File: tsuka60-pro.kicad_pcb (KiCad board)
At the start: 2 copper layers, 285 x 94.6 mm, 171 parts, among them J1 USB_C_Receptacle_USB2.0, J2 Conn_01x04_MountingPin, SW1 SW_Reset, U1 ATmega32U4-M, U2 SRV05-4, Y1 16MHz

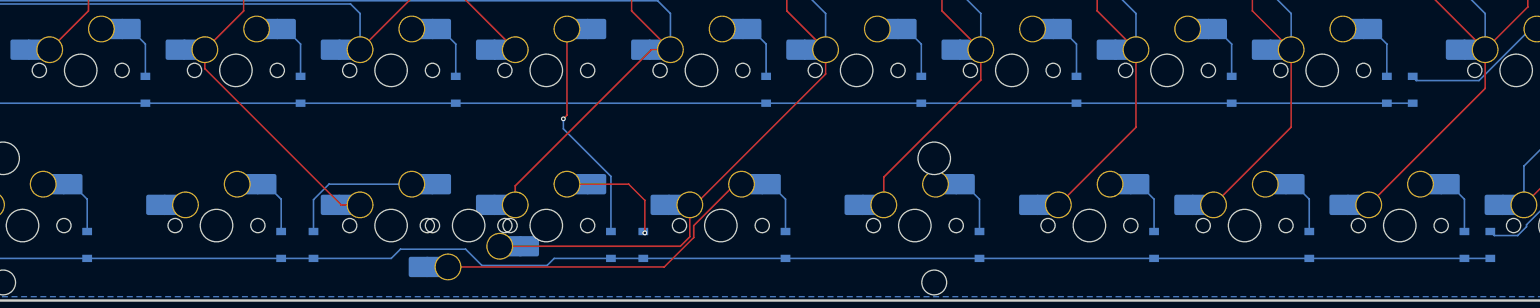
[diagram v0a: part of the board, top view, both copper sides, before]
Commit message: Add missing trace
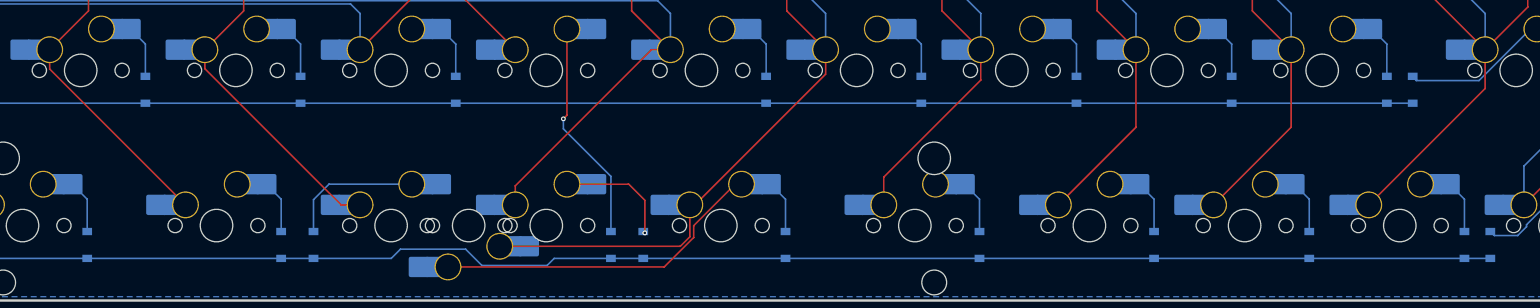
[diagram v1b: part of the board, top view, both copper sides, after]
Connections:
- MX66 pad 1: unconnected-(MX66-Pad1) -> COL5
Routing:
- net COL5: track 132.1 -> 158.1 mm

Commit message: Repair BOM, update USB-C component, footprint and placement
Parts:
- J1: footprint marbastlib-various:USB_C_Receptacle_HRO_TYPE-C-31-M-14 -> Connector_USB:USB_C_Receptacle_HRO_TYPE-C-31-M-12
- R3, R4: value 5k -> 5.1k
- moved J1 3.86 mm to (82.1, 82.2)
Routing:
- net GND: track 105.8 -> 95.2 mm, vias 2 -> 0
- net Net-(J1-PadA5): track 8.67 -> 12.4 mm
- net VCC: track 22.4 -> 24.0 mm
- net D+: track 36.5 -> 37.8 mm
- net Net-(J1-PadB5): track 8.40 -> 7.70 mm, vias 2 -> 0
- net D-: track 37.6 -> 38.1 mm
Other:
- outline, holes or cut-outs redrawn

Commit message: Update some traces
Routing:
- net Net-(D69-Pad2): track 14.6 -> 11.8 mm
- net COL9: track 294.7 -> 296.4 mm
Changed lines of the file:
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@@
   (segment (start 187.325 161.922183) (end 187.325 165.83125) (width 0.2) (layer "B.Cu") (net 65))
   (segment (start 199.39 160.02) (end 189.227183 160.02) (width 0.2) (layer "B.Cu") (net 65))
-  (segment (start 218.44 151.56) (end 218 152) (width 0.2) (layer "F.Cu") (net 66))
-  (segment (start 218.44 140.97) (end 218.44 151.56) (width 0.2) (layer "F.Cu") (net 66))
-  (via (at 218 152) (size 0.6) (drill 0.3) (layers "F.Cu" "B.Cu") (net 66))
-  (segment (start 223.8375 165.83125) (end 223.8375 159.064683) (width 0.2) (layer "B.Cu") (net 66))
-  (segment (start 223.8375 159.064683) (end 218 153.227183) (width 0.2) (layer "B.Cu") (net 66))
-  (segment (start 218 153.227183) (end 218 152) (width 0.2) (layer "B.Cu") (net 66))
-  (segment (start 228 162) (end 226.02 160.02) (width 0.2) (layer "F.Cu") (net 67))
-  (segment (start 228 166) (end 228 162) (width 0.2) (layer "F.Cu") (net 67))
-  (segment (start 226.02 160.02) (end 218.44 160.02) (width 0.2) (layer "F.Cu") (net 67))
-  (via (at 228 166) (size 0.6) (drill 0.3) (layers "F.Cu" "B.Cu") (net 67))
-  (segment (start 227.83125 165.83125) (end 228 166) (width 0.2) (layer "B.Cu") (net 67))
-  (segment (start 227.80625 165.83125) (end 227.83125 165.83125) (width 0.2) (layer "B.Cu") (net 67))
+  (segment (start 218.44 140.97) (end 218.44 151.46) (width 0.2) (layer "F.Cu") (net 66))
+  (segment (start 218.44 151.46) (end 218.44 151.94) (width 0.2) (layer "F.Cu") (net 66))
+  (via (at 218.44 151.94) (size 0.6) (drill 0.3) (layers "F.Cu" "B.Cu") (net 66))
+  (segment (start 223.8375 165.83125) (end 223.8375 159.6625) (width 0.2) (layer "B.Cu") (net 66))
+  (segment (start 223.8375 157.3375) (end 218.44 151.94) (width 0.2) (layer "B.Cu") (net 66))
+  (segment (start 223.8375 159.6625) (end 223.8375 157.3375) (width 0.2) (layer "B.Cu") (net 66))
+  (segment (start 218.44 160.02) (end 221.995 160.02) (width 0.2) (layer "F.Cu") (net 67))
+  (segment (start 221.995 160.02) (end 227.80625 165.83125) (width 0.2) (layer "F.Cu") (net 67))
+  (via (at 227.80625 165.83125) (size 0.6) (drill 0.3) (layers "F.Cu" "B.Cu") (net 67))
   (segment (start 326.765 160.02) (end 328.6125 161.8675) (width 0.2) (layer "B.Cu") (net 68))
   (segment (start 328.6125 161.8675) (end 328.6125 165.83125) (width 0.2) (layer "B.Cu") (net 68))
@@
   (segment (start 94.065686 137.5) (end 229.575 137.5) (width 0.2) (layer "B.Cu") (net 79))
   (segment (start 240.665 86.36) (end 240.665 105.41) (width 0.2) (layer "F.Cu") (net 80))
+  (segment (start 233.52125 166.47875) (end 230.22 169.78) (width 0.2) (layer "F.Cu") (net 80))
   (segment (start 234.142414 162.56) (end 250.19 146.512414) (width 0.2) (layer "F.Cu") (net 80))
+  (segment (start 212.325 169.78) (end 210.185 167.64) (width 0.2) (layer "F.Cu") (net 80))
+  (segment (start 233.52125 162.56) (end 233.52125 166.47875) (width 0.2) (layer "F.Cu") (net 80))
   (segment (start 240.665 119.6975) (end 245.4275 124.46) (width 0.2) (layer "F.Cu") (net 80))
-  (segment (start 233.52125 166.47875) (end 233.52125 162.56) (width 0.2) (layer "F.Cu") (net 80))
   (segment (start 233.52125 162.56) (end 234.142414 162.56) (width 0.2) (layer "F.Cu") (net 80))
-  (segment (start 232.36 167.64) (end 233.52125 166.47875) (width 0.2) (layer "F.Cu") (net 80))
   (segment (start 245.4275 138.7475) (end 250.19 143.51) (width 0.2) (layer "F.Cu") (net 80))
   (segment (start 240.665 105.41) (end 240.665 119.6975) (width 0.2) (layer "F.Cu") (net 80))
-  (segment (start 210.185 167.64) (end 232.36 167.64) (width 0.2) (layer "F.Cu") (net 80))
+  (segment (start 230.22 169.78) (end 212.325 169.78) (width 0.2) (layer "F.Cu") (net 80))
   (segment (start 245.4275 124.46) (end 245.4275 138.7475) (width 0.2) (layer "F.Cu") (net 80))
   (segment (start 250.19 146.512414) (end 250.19 143.51) (width 0.2) (layer "F.Cu") (net 80))
@@
   (segment (start 183.35625 161.8675) (end 183.35625 165.83125) (width 0.2) (layer "B.Cu") (net 111))
   (segment (start 181.50875 160.02) (end 183.35625 161.8675) (width 0.2) (layer "B.Cu") (net 111))
-  (segment (start 234 165.116473) (end 234 166.565686) (width 0.2) (layer "F.Cu") (net 112))
-  (segment (start 239.096473 160.02) (end 234 165.116473) (width 0.2) (layer "F.Cu") (net 112))
-  (segment (start 234 166.565686) (end 230.385686 170.18) (width 0.2) (layer "F.Cu") (net 112))
+  (segment (start 239.096473 160.02) (end 234.508236 164.608236) (width 0.2) (layer "F.Cu") (net 112))
+  (segment (start 234.508236 164.608236) (end 233.92125 165.195222) (width 0.2) (layer "F.Cu") (net 112))
+  (segment (start 233.92125 166.644436) (end 230.385686 170.18) (width 0.2) (layer "F.Cu") (net 112))
+  (segment (start 233.92125 165.195222) (end 233.92125 165.7) (width 0.2) (layer "F.Cu") (net 112))
+  (segment (start 233.92125 165.7) (end 233.92125 166.644436) (width 0.2) (layer "F.Cu") (net 112))
   (segment (start 239.87125 160.02) (end 239.096473 160.02) (width 0.2) (layer "F.Cu") (net 112))
   (segment (start 230.385686 170.18) (end 203.835 170.18) (width 0.2) (layer "F.Cu") (net 112))

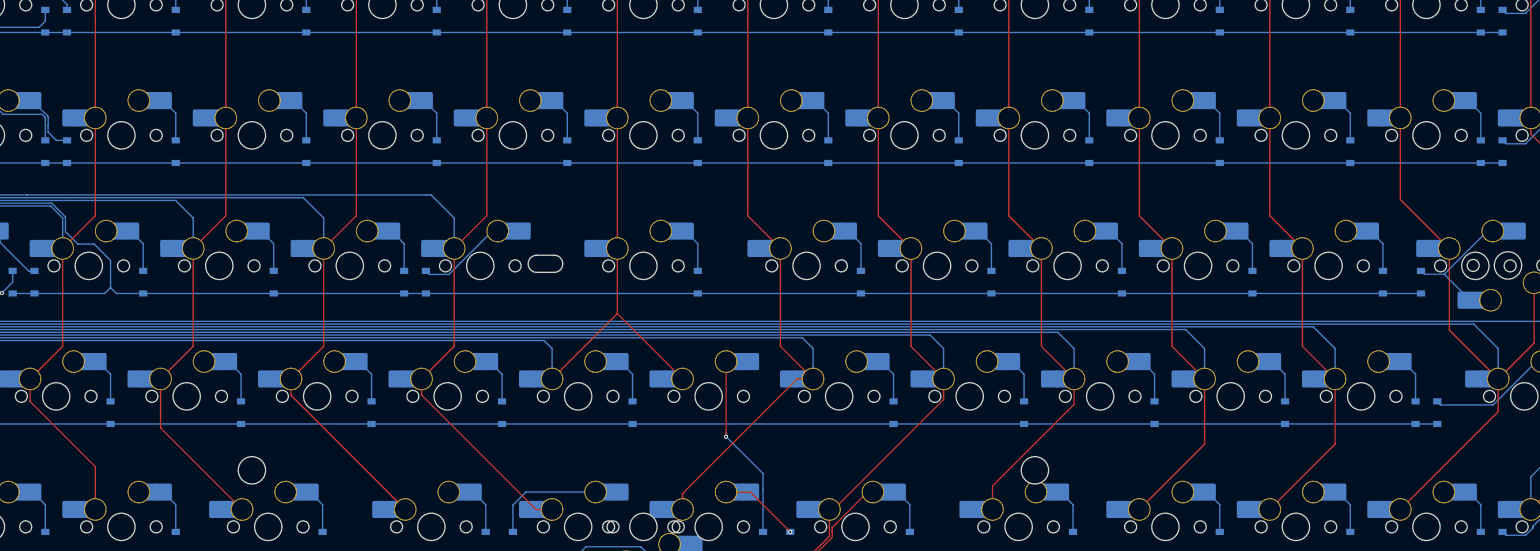
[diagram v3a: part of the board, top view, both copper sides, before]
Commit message: Add mounting holes and re-export productions files
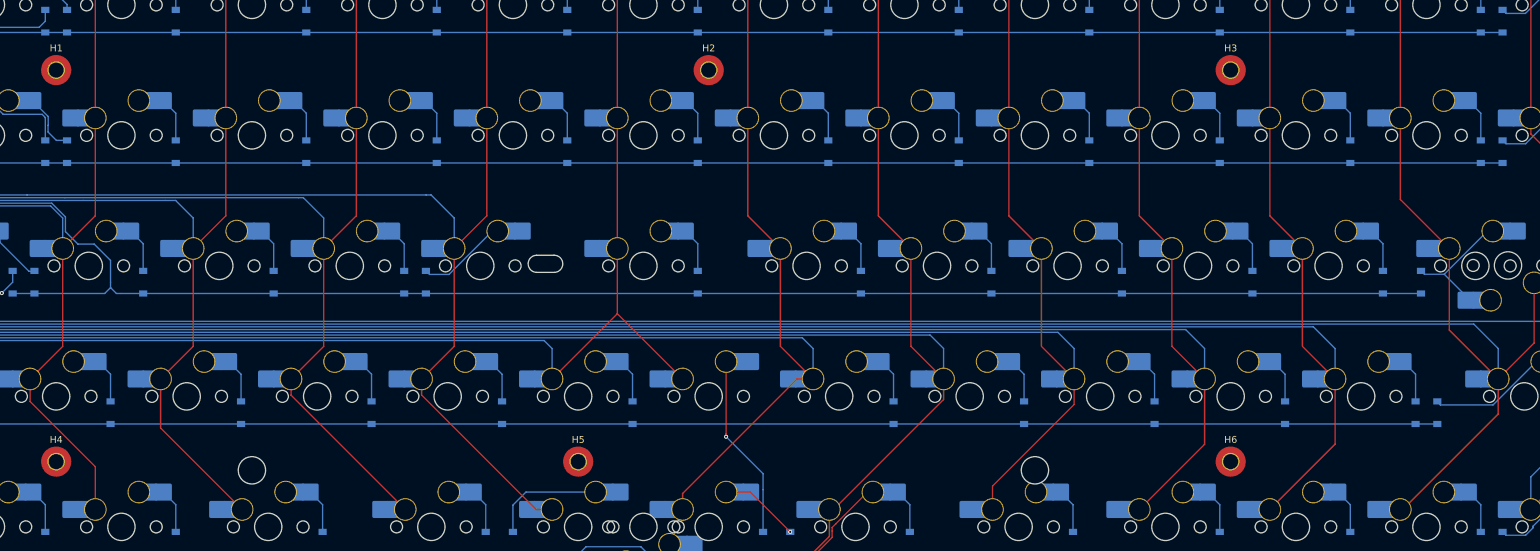
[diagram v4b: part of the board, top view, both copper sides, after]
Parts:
- added H1: MountingHole, MountingHole:MountingHole_2.2mm_M2_Pad_TopOnly, F.Cu at (120.7, 98.4)
- added H2: MountingHole, MountingHole:MountingHole_2.2mm_M2_Pad_TopOnly, F.Cu at (215.9, 98.4)
- added H3: MountingHole, MountingHole:MountingHole_2.2mm_M2_Pad_TopOnly, F.Cu at (292.1, 98.4)
- added H4: MountingHole, MountingHole:MountingHole_2.2mm_M2_Pad_TopOnly, F.Cu at (120.7, 155.6)
- added H5: MountingHole, MountingHole:MountingHole_2.2mm_M2_Pad_TopOnly, F.Cu at (196.8, 155.6)
- added H6: MountingHole, MountingHole:MountingHole_2.2mm_M2_Pad_TopOnly, F.Cu at (292.1, 155.6)
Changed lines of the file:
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@@
   (net 115 "unconnected-(U1-Pad9)")
   (net 116 "unconnected-(U1-Pad11)")
+  (footprint "MountingHole:MountingHole_2.2mm_M2_Pad_TopOnly" (layer "F.Cu")
+    (at 120.65 98.425)
+    (descr "Mounting Hole 2.2mm, M2")
+    (tags "mounting hole 2.2mm m2")
+    (property "Sheetfile" "File: tsuka60-pro.kicad_sch")
+    (property "Sheetname" "")
+    (attr exclude_from_pos_files)
+    (fp_text reference "H1" (at 0 -3.2) (layer "F.SilkS")
+      (effects (font (size 1 1) (thickness 0.15)))
+    )
+    (fp_text value "MountingHole" (at 0 3.2) (layer "F.Fab")
+      (effects (font (size 1 1) (thickness 0.15)))
+    )
+    (fp_text user "${REFERENCE}" (at 0 0) (layer "F.Fab")
+      (effects (font (size 1 1) (thickness 0.15)))
+    )
+    (fp_circle (center 0 0) (end 2.2 0) (layer "Cmts.User") (width 0.15) (fill none))
+    (fp_circle (center 0 0) (end 2.45 0) (layer "F.CrtYd") (width 0.05) (fill none))
+    (pad "1" connect circle (at 0 0) (size 4.4 4.4) (layers "F.Cu" "F.Mask"))
+    (pad "1" thru_hole circle (at 0 0) (size 2.6 2.6) (drill 2.2) (layers *.Cu *.Mask))
+  )
+  (footprint "MountingHole:MountingHole_2.2mm_M2_Pad_TopOnly" (layer "F.Cu")
+    (at 215.9 98.425)
+    (descr "Mounting Hole 2.2mm, M2")
+    (tags "mounting hole 2.2mm m2")
+    (property "Sheetfile" "File: tsuka60-pro.kicad_sch")
+    (property "Sheetname" "")
+    (attr exclude_from_pos_files)
+    (fp_text reference "H2" (at 0 -3.2) (layer "F.SilkS")
+      (effects (font (size 1 1) (thickness 0.15)))
+    )
+    (fp_text value "MountingHole" (at 0 3.2) (layer "F.Fab")
+      (effects (font (size 1 1) (thickness 0.15)))
+    )
+    (fp_text user "${REFERENCE}" (at 0 0) (layer "F.Fab")
+      (effects (font (size 1 1) (thickness 0.15)))
+    )
+    (fp_circle (center 0 0) (end 2.2 0) (layer "Cmts.User") (width 0.15) (fill none))
+    (fp_circle (center 0 0) (end 2.45 0) (layer "F.CrtYd") (width 0.05) (fill none))
+    (pad "1" thru_hole circle (at 0 0) (size 2.6 2.6) (drill 2.2) (layers *.Cu *.Mask))
+    (pad "1" connect circle (at 0 0) (size 4.4 4.4) (layers "F.Cu" "F.Mask"))
+  )
+  (footprint "MountingHole:MountingHole_2.2mm_M2_Pad_TopOnly" (layer "F.Cu")
+    (at 196.85 155.575)
+    (descr "Mounting Hole 2.2mm, M2")
+    (tags "mounting hole 2.2mm m2")
+    (property "Sheetfile" "File: tsuka60-pro.kicad_sch")
+    (property "Sheetname" "")
+    (attr exclude_from_pos_files)
+    (fp_text reference "H5" (at 0 -3.2) (layer "F.SilkS")
+      (effects (font (size 1 1) (thickness 0.15)))
+    )
+    (fp_text value "MountingHole" (at 0 3.2) (layer "F.Fab")
+      (effects (font (size 1 1) (thickness 0.15)))
+    )
+    (fp_text user "${REFERENCE}" (at 0 0) (layer "F.Fab")
+      (effects (font (size 1 1) (thickness 0.15)))
+    )
+    (fp_circle (center 0 0) (end 2.2 0) (layer "Cmts.User") (width 0.15) (fill none))
+    (fp_circle (center 0 0) (end 2.45 0) (layer "F.CrtYd") (width 0.05) (fill none))
+    (pad "1" connect circle (at 0 0) (size 4.4 4.4) (layers "F.Cu" "F.Mask"))
+    (pad "1" thru_hole circle (at 0 0) (size 2.6 2.6) (drill 2.2) (layers *.Cu *.Mask))
+  )
   (footprint "marbastlib-mx:STAB_MX_7u" (layer "F.Cu")
     (at 206.375 165.1 180)
@@
     )
   )
+  (footprint "MountingHole:MountingHole_2.2mm_M2_Pad_TopOnly" (layer "F.Cu")
+    (at 292.1 155.575)
+    (descr "Mounting Hole 2.2mm, M2")
+    (tags "mounting hole 2.2mm m2")
+    (property "Sheetfile" "File: tsuka60-pro.kicad_sch")
+    (property "Sheetname" "")
+    (attr exclude_from_pos_files)
+    (fp_text reference "H6" (at 0 -3.2) (layer "F.SilkS")
+      (effects (font (size 1 1) (thickness 0.15)))
+    )
+    (fp_text value "MountingHole" (at 0 3.2) (layer "F.Fab")
+      (effects (font (size 1 1) (thickness 0.15)))
+    )
+    (fp_text user "${REFERENCE}" (at 0 0) (layer "F.Fab")
+      (effects (font (size 1 1) (thickness 0.15)))
+    )
+    (fp_circle (center 0 0) (end 2.2 0) (layer "Cmts.User") (width 0.15) (fill none))
+    (fp_circle (center 0 0) (end 2.45 0) (layer "F.CrtYd") (width 0.05) (fill none))
+    (pad "1" connect circle (at 0 0) (size 4.4 4.4) (layers "F.Cu" "F.Mask"))
+    (pad "1" thru_hole circle (at 0 0) (size 2.6 2.6) (drill 2.2) (layers *.Cu *.Mask))
+  )
+  (footprint "MountingHole:MountingHole_2.2mm_M2_Pad_TopOnly" (layer "F.Cu")
+    (at 120.65 155.575)
+    (descr "Mounting Hole 2.2mm, M2")
+    (tags "mounting hole 2.2mm m2")
+    (property "Sheetfile" "File: tsuka60-pro.kicad_sch")
+    (property "Sheetname" "")
+    (attr exclude_from_pos_files)
+    (fp_text reference "H4" (at 0 -3.2) (layer "F.SilkS")
+      (effects (font (size 1 1) (thickness 0.15)))
+    )
+    (fp_text value "MountingHole" (at 0 3.2) (layer "F.Fab")
+      (effects (font (size 1 1) (thickness 0.15)))
+    )
+    (fp_text user "${REFERENCE}" (at 0 0) (layer "F.Fab")
+      (effects (font (size 1 1) (thickness 0.15)))
+    )
+    (fp_circle (center 0 0) (end 2.2 0) (layer "Cmts.User") (width 0.15) (fill none))
+    (fp_circle (center 0 0) (end 2.45 0) (layer "F.CrtYd") (width 0.05) (fill none))
+    (pad "1" connect circle (at 0 0) (size 4.4 4.4) (layers "F.Cu" "F.Mask"))
+    (pad "1" thru_hole circle (at 0 0) (size 2.6 2.6) (drill 2.2) (layers *.Cu *.Mask))
+  )
   (footprint "locallib:60_Outline-Modded" locked (layer "F.Cu")
     (at 206.375 127)
@@
     (fp_arc (start 137.3 9.2) (mid 137.710051 8.210051) (end 138.7 7.8) (layer "Edge.Cuts") (width 0.3))
   )
+  (footprint "MountingHole:MountingHole_2.2mm_M2_Pad_TopOnly" (layer "F.Cu")
+    (at 292.1 98.425)
+    (descr "Mounting Hole 2.2mm, M2")
+    (tags "mounting hole 2.2mm m2")
+    (property "Sheetfile" "File: tsuka60-pro.kicad_sch")
+    (property "Sheetname" "")
+    (attr exclude_from_pos_files)
+    (fp_text reference "H3" (at 0 -3.2) (layer "F.SilkS")
+      (effects (font (size 1 1) (thickness 0.15)))
+    )
+    (fp_text value "MountingHole" (at 0 3.2) (layer "F.Fab")
+      (effects (font (size 1 1) (thickness 0.15)))
+    )
+    (fp_text user "${REFERENCE}" (at 0 0) (layer "F.Fab")
+      (effects (font (size 1 1) (thickness 0.15)))
+    )
+    (fp_circle (center 0 0) (end 2.2 0) (layer "Cmts.User") (width 0.15) (fill none))
+    (fp_circle (center 0 0) (end 2.45 0) (layer "F.CrtYd") (width 0.05) (fill none))
+    (pad "1" connect circle (at 0 0) (size 4.4 4.4) (layers "F.Cu" "F.Mask"))
+    (pad "1" thru_hole circle (at 0 0) (size 2.6 2.6) (drill 2.2) (layers *.Cu *.Mask))
+  )
   (footprint "marbastlib-mx:SW_MX_HS_1u" (layer "B.Cu")
     (at 273.05 146.05 180)
@@
   (segment (start 336.39125 129.4775) (end 336.39125 138.27125) (width 0.2) (layer "F.Cu") (net 81))
   (segment (start 324.00875 136.36625) (end 331.1525 143.51) (width 0.2) (layer "F.Cu") (net 81))
-  (segment (start 331.1525 148.2725) (end 316.865 162.56) (width 0.2) (layer "F.Cu") (net 81))
+  (segment (start 331.1525 143.51) (end 331.1525 148.633034) (width 0.2) (layer "F.Cu") (net 81))
   (segment (start 324.00875 124.46) (end 324.00875 136.36625) (width 0.2) (layer "F.Cu") (net 81))
   (segment (start 336.39125 138.27125) (end 331.1525 143.51) (width 0.2) (layer "F.Cu") (net 81))
   (segment (start 316.865 117.31625) (end 324.00875 124.46) (width 0.2) (layer "F.Cu") (net 81))
   (segment (start 316.865 86.36) (end 316.865 105.41) (width 0.2) (layer "F.Cu") (net 81))
-  (segment (start 331.1525 143.51) (end 331.1525 148.2725) (width 0.2) (layer "F.Cu") (net 81))
+  (segment (start 317.225534 162.56) (end 316.865 162.56) (width 0.2) (layer "F.Cu") (net 81))
+  (segment (start 331.1525 148.633034) (end 317.225534 162.56) (width 0.2) (layer "F.Cu") (net 81))
   (segment (start 92.28125 120.4375) (end 92.28125 124.321448) (width 0.2) (layer "B.Cu") (net 81))
   (segment (start 94.9 135.5) (end 327.5875 135.5) (width 0.2) (layer "B.Cu") (net 81))
